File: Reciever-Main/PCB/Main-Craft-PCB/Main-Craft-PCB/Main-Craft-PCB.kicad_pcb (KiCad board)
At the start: 2 copper layers, 96 parts, among them SW4 SW_SPDT, SW5 SW_SPDT, SW6 SW_SPDT, SW7 SW_SPDT, SW8 SW_SPDT, U1 NUCLEO144-F429ZI, U2 LM741, U3 LM741, U4 LM2940-3.0, U5 LM2940-5.0, U6 LM2940-12.0

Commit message: Update PCB and start pon layout
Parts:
- removed R20, R23, R29: 1K, Resistor_SMD:R_0603_1608Metric
- removed R22, R24, R26: 10K, Resistor_SMD:R_0603_1608Metric
- added BT1: Battery, Connector_PinHeader_2.54mm:PinHeader_1x02_P2.54mm_Vertical, F.Cu at (124.5, 55.9)
- added D14: 1N5817, My_library:1N5817M, F.Cu at (55.9, 27.9)
- added J1: nRF24L01_Conn, Connector_PinHeader_2.54mm:PinHeader_2x04_P2.54mm_Vertical_SMD, F.Cu at (170.1, 57.6)
- added J10: L298N, Connector_PinHeader_2.54mm:PinHeader_1x06_P2.54mm_Vertical_SMD_Pin1Left, F.Cu at (124.5, 139.7)
- added J2: IR_SENSOR_1, Connector_PinHeader_2.54mm:PinHeader_1x03_P2.54mm_Vertical_SMD_Pin1Left, F.Cu at (139.7, 144.8)
- added J3: IR_SENSOR_2, Connector_PinHeader_2.54mm:PinHeader_1x03_P2.54mm_Vertical_SMD_Pin1Left, F.Cu at (147.3, 144.8)
- added J4: IR_SENSOR_?, Connector_PinHeader_2.54mm:PinHeader_1x03_P2.54mm_Vertical_SMD_Pin1Left, F.Cu at (132.1, 144.8)
- added J5: IR_SENSOR_?, Connector_PinHeader_2.54mm:PinHeader_1x03_P2.54mm_Vertical_SMD_Pin1Left, F.Cu at (154.9, 144.7)
- added J6: ESC_1, Connector_PinHeader_2.54mm:PinHeader_1x03_P2.54mm_Vertical_SMD_Pin1Left, F.Cu at (185.4, 144.8)
- added J7: ESC_2, Connector_PinHeader_2.54mm:PinHeader_1x03_P2.54mm_Vertical_SMD_Pin1Left, F.Cu at (177.8, 144.8)
- added J8: ESC_3, Connector_PinHeader_2.54mm:PinHeader_1x03_P2.54mm_Vertical_SMD_Pin1Left, F.Cu at (170.2, 144.8)
- added J9: ESC_4, Connector_PinHeader_2.54mm:PinHeader_1x03_P2.54mm_Vertical_SMD_Pin1Left, F.Cu at (162.6, 144.8)
- added Q1: 2N2219, Package_TO_SOT_SMD:SOT-23, F.Cu at (16.1, 15.2)
- added Q10: 2N2219, Package_TO_SOT_SMD:SOT-23, F.Cu at (33.0, 66.0)
- added Q11: 2N2219, Package_TO_SOT_SMD:SOT-23, F.Cu at (84.8, 37.1)
- added Q12: 2N2219, Package_TO_SOT_SMD:SOT-23, F.Cu at (97.5, 39.7)
- added Q13: 2N2219, Package_TO_SOT_SMD:SOT-23, F.Cu at (-82.1, 63.5)
- added Q14: 2N2219, Package_TO_SOT_SMD:SOT-23, F.Cu at (-55.9, 30.5)
- added Q2: 2N2219, Package_TO_SOT_SMD:SOT-23, F.Cu at (33.0, 15.2)
- added Q3: 2N2219, Package_TO_SOT_SMD:SOT-23, F.Cu at (16.0, 27.9)
- added Q4: 2N2219, Package_TO_SOT_SMD:SOT-23, F.Cu at (33.0, 22.9)
- added Q5: 2N2219, Package_TO_SOT_SMD:SOT-23, F.Cu at (20.3, 35.6)
- added Q6: 2N2219, Package_TO_SOT_SMD:SOT-23, F.Cu at (35.6, 33.0)
- added Q7: 2N2219, Package_TO_SOT_SMD:SOT-23, F.Cu at (17.8, 45.7)
- added Q8: 2N2219, Package_TO_SOT_SMD:SOT-23, F.Cu at (20.3, 58.4)
- added Q9: 2N2219, Package_TO_SOT_SMD:SOT-23, F.Cu at (35.6, 48.3)
- added SW1: SW_Push, Button_Switch_SMD:SW_Push_1P1T_NO_6x6mm_H9.5mm, F.Cu at (167.6, 68.6)
- added SW2: SW_Push, Button_Switch_SMD:SW_Push_1P1T_NO_6x6mm_H9.5mm, F.Cu at (167.6, 76.2)
- D17: footprint My_library:1N5817M -> Diode_SMD:D_0603_1608Metric
- SW4, SW5, SW6, SW7, SW8: footprint My_library:KNX-1-D1 -> My_library:JS202011SCQN
- U1: footprint Module:ST_Morpho_Connector_144_STLink -> My_library:MODULE_NUCLEO-F429ZI
- U6: footprint My_library:KNX-1-D1 -> Package_TO_SOT_SMD:SOT-223
- moved R39 229.8 mm to (-72.7, 63.5)
- moved R43 222.7 mm to (-77.8, 66.0)
- moved R49 209.1 mm to (-71.9, 55.9)
- moved C1 207.1 mm to (-55.9, 63.5)
- moved R50 200.8 mm to (-48.3, 43.2)
- moved U2 198.2 mm to (-64.3, 58.4)
- moved C3 196.5 mm to (-64.3, 63.5)
- moved D12 193.1 mm to (-77.0, 58.4)
- moved R44 184.3 mm to (-59.2, 53.3)
- moved R45 183.2 mm to (-48.3, 30.5)
- moved D13 178.5 mm to (-61.0, 38.1)
- moved C2 176.0 mm to (-54.1, 43.2)
- moved RV2 175.3 mm to (-52.2, 36.5)
- moved RV1 170.7 mm to (-54.1, 58.4)
- moved R46 170.2 mm to (-44.0, 27.9)
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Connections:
- R27 pad 2: SW_4 -> SW_5
- R31 pad 2: SW_7 -> SW_4
- R34 pad 2: SW_5 -> SW_6
- R38 pad 2: SW_6 -> SW_5
- U1 pad 125: SW_7 -> unconnected-(U1-Pad125)
- U1 pad 46: MOTOR_2_A -> unconnected-(U1-Pad46)
- U1 pad 47: unconnected-(U1-Pad47) -> MOTOR_2_A
- U1 pad 90: SW_9 -> unconnected-(U1-Pad90)
- U1 pad 97: SW_8 -> unconnected-(U1-Pad97)
- U1 pad 99: MOSI -> MISO
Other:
- board outline added: 68.6 x 99.1 mm

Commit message: Start Routing for tracks on PCB
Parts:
- removed the SW5 at (167.6, 96.5)
- added R20: 1K, Resistor_SMD:R_0603_1608Metric, F.Cu at (172.7, 97.8)
- added R22: 10K, Resistor_SMD:R_0603_1608Metric, F.Cu at (172.7, 94.6)
- added R23: 10K, Resistor_SMD:R_0603_1608Metric, F.Cu at (162.6, 94.6)
- added R24: 1K, Resistor_SMD:R_0603_1608Metric, F.Cu at (162.6, 97.8)
- added SW6: SW_SPDT, My_library:JS202011SCQN, F.Cu at (167.6, 95.9)
- J10: footprint Connector_PinHeader_2.54mm:PinHeader_1x06_P2.54mm_Vertical_SMD_Pin1Left -> Connector_PinHeader_2.54mm:PinHeader_1x06_P2.54mm_Vertical
- J2, J3, J4, J5, J6, J7, J8, J9: footprint Connector_PinHeader_2.54mm:PinHeader_1x03_P2.54mm_Vertical_SMD_Pin1Left -> Connector_PinHeader_2.54mm:PinHeader_1x03_P2.54mm_Vertical
- SW8: footprint My_library:JS202011SCQN -> My_library:KNX-1-D1
- U1: footprint My_library:MODULE_NUCLEO-F429ZI -> My_library:MODULE_NUCLEO-F429ZI_JUST_PINS
- moved Q13 235.9 mm to (153.0, 82.5), turned to 180 degrees
- moved D12 235.7 mm to (158.1, 74.9), turned to 90 degrees
- moved R49 231.1 mm to (158.1, 78.7), turned to -90 degrees
- moved R43 224.6 mm to (146.1, 84.5), turned to 90 degrees
- moved R39 222.3 mm to (149.2, 76.8), turned to 90 degrees
- moved U2 218.8 mm to (153.7, 78.1)
- moved C3 214.2 mm to (149.2, 80.6), turned to 90 degrees
- moved R44 210.7 mm to (149.2, 84.5), turned to 90 degrees
- moved D13 209.5 mm to (145.4, 74.3), turned to 90 degrees
- moved RV1 207.7 mm to (153.0, 72.9), turned to -90 degrees
- moved C1 205.3 mm to (149.2, 72.9), turned to 90 degrees
- moved Q14 202.8 mm to (140.3, 81.9), turned to 180 degrees
- moved R50 196.8 mm to (145.4, 78.1), turned to -90 degrees
- moved RV2 196.2 mm to (140.7, 72.3), turned to -90 degrees
- moved C2 193.5 mm to (137.2, 72.4), turned to -90 degrees
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- renumbered SW6 to SW3, SW7 to SW5
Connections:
- R31 pad 2: SW_4 -> SW_3
- R38 pad 2: SW_5 -> SW_4
- SW4 pad 1: Net-(R26-Pad1) -> unconnected-(SW4-Pad1)
- SW4 pad 3: Net-(R23-Pad1) -> Net-(R27-Pad1)
- U1 pad 109: unconnected-(U1-Pad109) -> BAT_15_PERCENT
- U1 pad 115: BAT_15_PERCENT -> unconnected-(U1-Pad115)
- U1 pad 117: BAT_30_PERCENT -> unconnected-(U1-Pad117)
- U1 pad 122: unconnected-(U1-Pad122) -> SW_7
- U1 pad 127: unconnected-(U1-Pad127) -> SW_8
- U1 pad 38: unconnected-(U1-Pad38) -> BAT_30_PERCENT
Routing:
- net +5V: track 0.00 -> 476.2 mm, vias 0 -> 9
- net +BATT: track 0.00 -> 119.6 mm, vias 0 -> 4
- net BUZZER: track 0.00 -> 80.4 mm
- net MOTOR_1_EN: track 0.00 -> 62.0 mm
- net +3V3: track 0.00 -> 57.7 mm, vias 0 -> 2
- net SW_1: track 0.00 -> 51.6 mm, vias 0 -> 1
- net +12V: track 0.00 -> 50.9 mm
- net SW_4: track 0.00 -> 50.6 mm, vias 0 -> 1
- net SW_2: track 0.00 -> 48.1 mm
- net IR_4: track 0.00 -> 47.8 mm
- net IR_3: track 0.00 -> 46.3 mm
- net Net-(Q6-Pad3): track 0.00 -> 45.8 mm
- net IR_2: track 0.00 -> 44.6 mm
- net IR_1: track 0.00 -> 43.9 mm
- net Net-(Q5-Pad3): track 0.00 -> 39.6 mm
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- added copper zone on B.Cu, net Earth
- added copper zone on F.Cu, net Earth

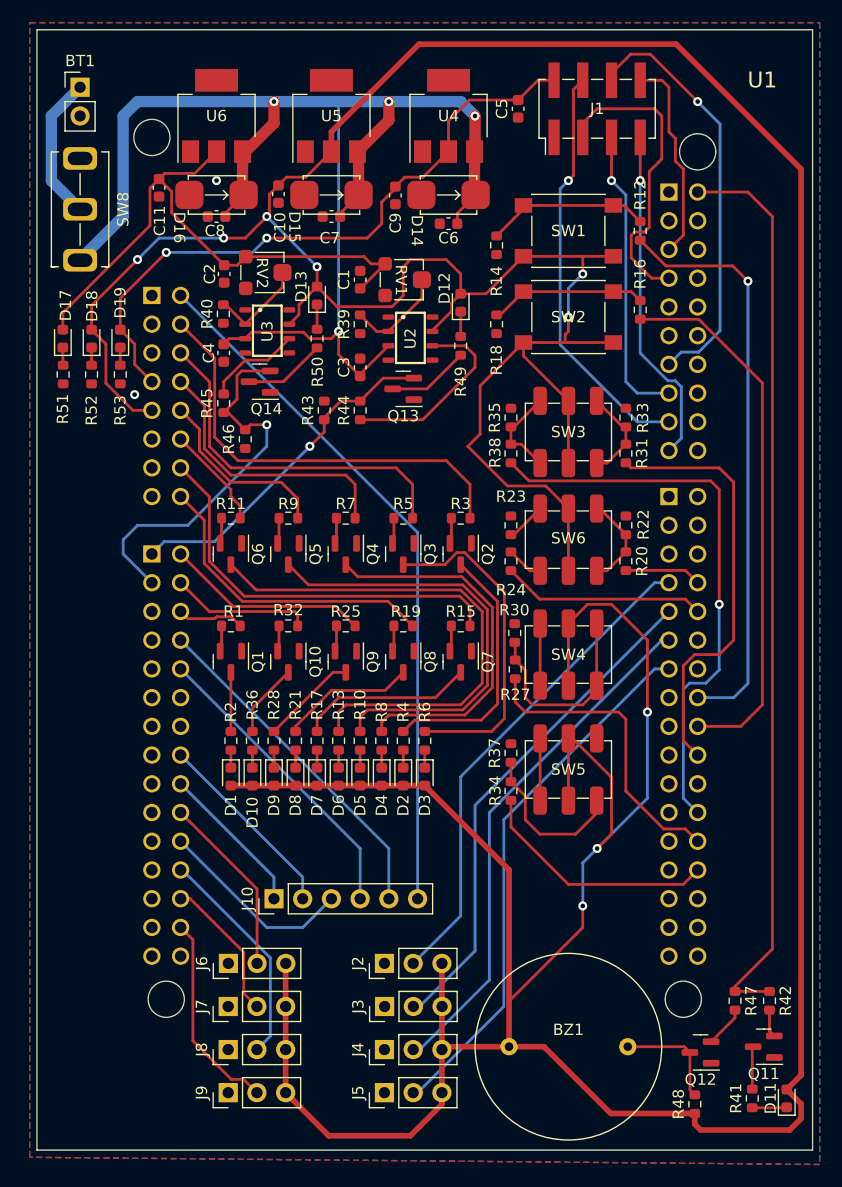
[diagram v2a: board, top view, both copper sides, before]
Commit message: Clear DRC for the PCB
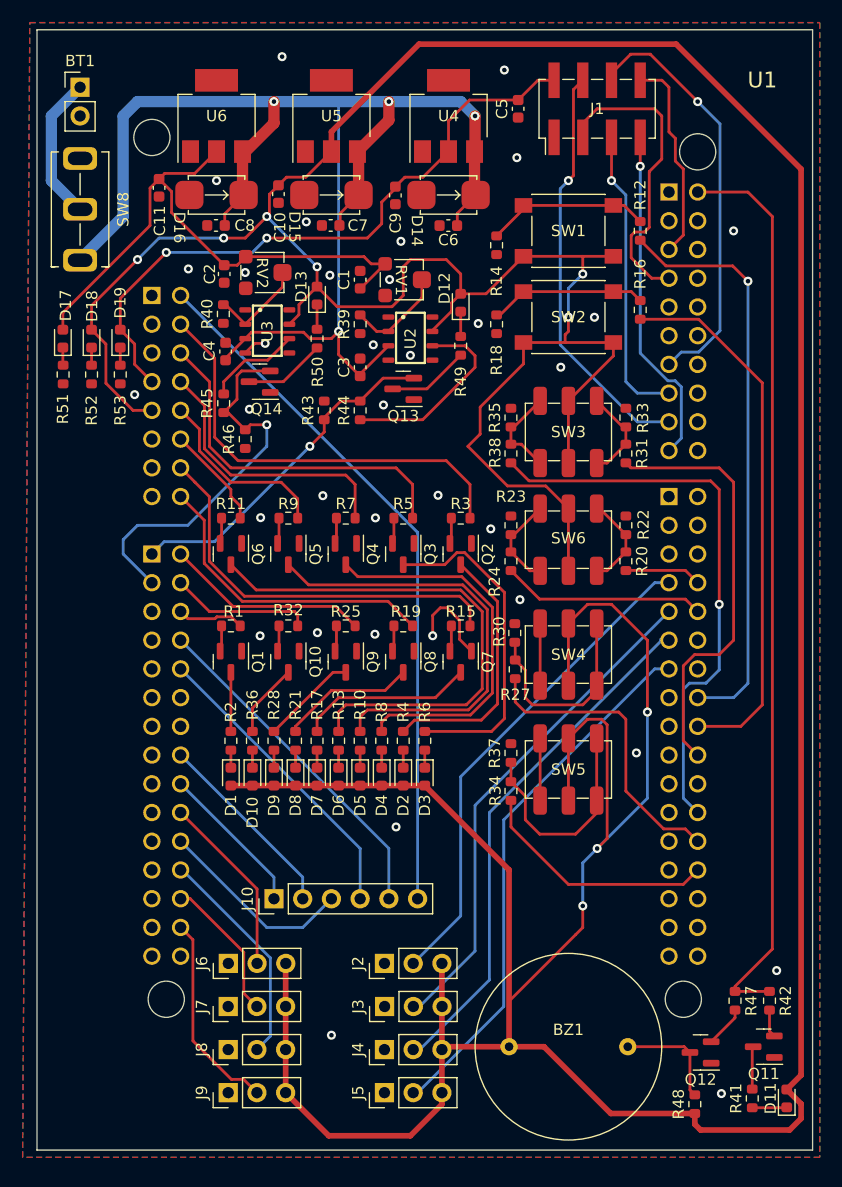
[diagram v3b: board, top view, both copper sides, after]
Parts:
- moved C7 0.79 mm to (146.6, 68.1)
- moved C8 0.79 mm to (136.5, 68.1)
- moved C4 0.21 mm to (137.3, 79.2), turned to 90 degrees
- moved C6 0.17 mm to (157.0, 68.1)
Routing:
- net Earth: track 0.00 -> 10.2 mm, vias 2 -> 35
- net Net-(R34-Pad1): track 14.3 -> 19.8 mm
- net +5V: track 476.2 -> 479.7 mm
- net +BATT: track 119.6 -> 121.7 mm
- net Net-(R23-Pad1): track 6.81 -> 8.06 mm
- net Net-(BT1-Pad1): track 13.5 -> 12.9 mm

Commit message: Finalise PCB
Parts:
- renumbered SW8 to PWR, BT1 to PWR
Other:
- board text added: "+"
- board text added: "-"
- board text added: "0"
- board text added: "1"
- board text added: "12V"
- board text added: "1A"
- board text added: "1B"
- board text added: "1_EN"
- board text added: "2"
- board text added: "2A"
- board text added: "2B"
- board text added: "2_EN"
- board text added: "3"
- board text added: "3V3"
- board text added: "4"
- board text added: "5V"
- board text added: "NUCLEO-F429ZI"
- board text added: "O.R.C.A - Main Board"
- board text added: "nRF24L01"
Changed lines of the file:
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@@
     (property "Sheetname" "")
     (attr through_hole)
-    (fp_text reference "SW8" (at 0 3.81 90 unlocked) (layer "F.SilkS")
+    (fp_text reference "PWR" (at 0 5.08 90 unlocked) (layer "F.SilkS")
       (effects (font (size 1 1) (thickness 0.15)))
     )
@@
     (property "Sheetname" "")
     (attr smd)
-    (fp_text reference "D17" (at 2.933761 0.251495 90) (layer "F.SilkS")
+    (fp_text reference "D17" (at 3.025708 0.007025 90) (layer "F.SilkS")
       (effects (font (size 1 1) (thickness 0.15)))
     )
@@
     (property "Sheetname" "")
     (attr through_hole)
-    (fp_text reference "J4" (at 0 -2.33 90) (layer "F.SilkS")
+    (fp_text reference "J4" (at 0 7.597562 90) (layer "F.SilkS")
       (effects (font (size 1 1) (thickness 0.15)))
     )
@@
     (property "Sheetname" "")
     (attr through_hole)
-    (fp_text reference "J8" (at 0 -2.33 90) (layer "F.SilkS")
+    (fp_text reference "J8" (at -0.031528 -2.442763 90) (layer "F.SilkS")
       (effects (font (size 1 1) (thickness 0.15)))
     )
@@
     (property "Sheetname" "")
     (attr through_hole)
-    (fp_text reference "J2" (at 0 -2.33 90) (layer "F.SilkS")
+    (fp_text reference "J2" (at 0 8.01101 90) (layer "F.SilkS")
       (effects (font (size 1 1) (thickness 0.15)))
     )
@@
     (property "Sheetname" "")
     (attr through_hole)
-    (fp_text reference "J9" (at 0 -2.33 90) (layer "F.SilkS")
+    (fp_text reference "J9" (at 0.006773 -2.48048 90) (layer "F.SilkS")
       (effects (font (size 1 1) (thickness 0.15)))
     )
@@
     (property "Sheetname" "")
     (attr through_hole)
-    (fp_text reference "U1" (at 29.845 -43.815) (layer "F.SilkS")
+    (fp_text reference "U1" (at 29.21 -36.195) (layer "F.SilkS")
       (effects (font (size 1.4 1.4) (thickness 0.15)))
     )
@@
     (property "Sheetname" "")
     (attr through_hole)
-    (fp_text reference "BT1" (at 0 -2.33) (layer "F.SilkS")
+    (fp_text reference "PWR" (at 0 -2.54) (layer "F.SilkS")
       (effects (font (size 1 1) (thickness 0.15)))
     )
@@
     (property "Sheetname" "")
     (attr smd)
-    (fp_text reference "C6" (at 0 1.27) (layer "F.SilkS")
+    (fp_text reference "C6" (at -0.016334 1.51793) (layer "F.SilkS")
       (effects (font (size 1 1) (thickness 0.15)))
     )
@@
     (property "Sheetname" "")
     (attr through_hole)
-    (fp_text reference "J5" (at 0 -2.33 90) (layer "F.SilkS")
+    (fp_text reference "J5" (at 0 7.696792 90) (layer "F.SilkS")
       (effects (font (size 1 1) (thickness 0.15)))
     )
@@
     (property "Sheetname" "")
     (attr smd)
-    (fp_text reference "D18" (at 2.875538 0.043045 90) (layer "F.SilkS")
+    (fp_text reference "D18" (at 3.176312 0.043045 90) (layer "F.SilkS")
       (effects (font (size 1 1) (thickness 0.15)))
     )
@@
     (property "Sheetname" "")
     (attr through_hole)
-    (fp_text reference "J7" (at 0 -2.33 90) (layer "F.SilkS")
+    (fp_text reference "J7" (at 0.043323 -2.405046 90) (layer "F.SilkS")
       (effects (font (size 1 1) (thickness 0.15)))
     )
@@
     (property "Sheetname" "")
     (attr smd)
-    (fp_text reference "D13" (at 0.780778 -1.397764 90) (layer "F.SilkS")
+    (fp_text reference "D13" (at 0.865916 -1.610494 90) (layer "F.SilkS")
       (effects (font (size 1 1) (thickness 0.15)))
     )
@@
     (property "Sheetname" "")
     (attr through_hole)
-    (fp_text reference "J3" (at 0 -2.33 90) (layer "F.SilkS")
+    (fp_text reference "J3" (at 0 7.99601 90) (layer "F.SilkS")
       (effects (font (size 1 1) (thickness 0.15)))
     )
@@
     (property "Sheetname" "")
     (attr through_hole)
-    (fp_text reference "J6" (at 0 -2.33 90) (layer "F.SilkS")
+    (fp_text reference "J6" (at 0.005023 -2.49548 90) (layer "F.SilkS")
       (effects (font (size 1 1) (thickness 0.15)))
     )
@@
     (property "Sheetname" "")
     (attr smd)
-    (fp_text reference "R24" (at 1.806736 1.442446 90) (layer "F.SilkS")
+    (fp_text reference "R24" (at 2.54 0 180) (layer "F.SilkS")
       (effects (font (size 1 1) (thickness 0.15)))
     )
@@
   )
   (gr_rect (start 120.65 50.8) (end 189.23 149.86) (layer "Edge.Cuts") (width 0.1) (fill none))
+  (gr_text "2B" (at 144.165975 130.5106) (layer "F.SilkS")
+    (effects (font (size 1.5 1.5) (thickness 0.3)))
+  )
+  (gr_text "-" (at 127.635 58.42) (layer "F.SilkS")
+    (effects (font (size 1.5 1.5) (thickness 0.3)))
+  )
+  (gr_text "1" (at 148.59 133.35) (layer "F.SilkS")
+    (effects (font (size 1.5 1.5) (thickness 0.3)))
+  )
+  (gr_text "1_EN" (at 155.555428 130.531575) (layer "F.SilkS")
+    (effects (font (size 1.5 1.5) (thickness 0.3)))
+  )
+  (gr_text "O.R.C.A - Main Board" (at 125.095 111.76 90) (layer "F.SilkS")
+    (effects (font (size 1.5 1.5) (thickness 0.3)))
+  )
+  (gr_text "2A" (at 146.685 124.46) (layer "F.SilkS")
+    (effects (font (size 1.5 1.5) (thickness 0.3)))
+  )
+  (gr_text "3" (at 145.415 140.97) (layer "F.SilkS")
+    (effects (font (size 1.5 1.5) (thickness 0.3)))
+  )
+  (gr_text "+\n" (at 127.635 55.88 90) (layer "F.SilkS")
+    (effects (font (size 1.5 1.5) (thickness 0.3)))
+  )
+  (gr_text "5V" (at 146.685 52.705) (layer "F.SilkS")
+    (effects (font (size 1.5 1.5) (thickness 0.3)))
+  )
+  (gr_text "1A" (at 151.765 124.46) (layer "F.SilkS")
+    (effects (font (size 1.5 1.5) (thickness 0.3)))
+  )
+  (gr_text "NUCLEO-F429ZI" (at 182.88 116.84 90) (layer "F.SilkS")
+    (effects (font (size 1.5 1.5) (thickness 0.3)))
+  )
+  (gr_text "2" (at 148.59 137.16) (layer "F.SilkS")
+    (effects (font (size 1.5 1.5) (thickness 0.3)))
+  )
+  (gr_text "3V3" (at 156.845 52.705) (layer "F.SilkS")
+    (effects (font (size 1.5 1.5) (thickness 0.3)))
+  )
+  (gr_text "1B" (at 149.325837 130.489625) (layer "F.SilkS")
+    (effects (font (size 1.5 1.5) (thickness 0.3)))
+  )
+  (gr_text "-\n" (at 128.27 66.675 90) (layer "F.SilkS")
+    (effects (font (size 1.5 1.5) (thickness 0.3)))
+  )
+  (gr_text "1" (at 128.27 70.485) (layer "F.SilkS")
+    (effects (font (size 1.5 1.5) (thickness 0.3)))
+  )
+  (gr_text "2" (at 145.415 137.16) (layer "F.SilkS")
+    (effects (font (size 1.5 1.5) (thickness 0.3)))
+  )
+  (gr_text "12V" (at 136.525 52.705) (layer "F.SilkS")
+    (effects (font (size 1.5 1.5) (thickness 0.3)))
+  )
+  (gr_text "4" (at 145.415 144.78) (layer "F.SilkS")
+    (effects (font (size 1.5 1.5) (thickness 0.3)))
+  )
+  (gr_text "1" (at 145.415 133.35) (layer "F.SilkS")
+    (effects (font (size 1.5 1.5) (thickness 0.3)))
+  )
+  (gr_text "0" (at 128.27 62.23) (layer "F.SilkS")
+    (effects (font (size 1.5 1.5) (thickness 0.3)))
+  )
+  (gr_text "2_EN" (at 140.97 124.46) (layer "F.SilkS")
+    (effects (font (size 1.5 1.5) (thickness 0.3)))
+  )
+  (gr_text "4" (at 148.59 144.78) (layer "F.SilkS")
+    (effects (font (size 1.5 1.5) (thickness 0.3)))
+  )
+  (gr_text "3" (at 148.59 140.97) (layer "F.SilkS")
+    (effects (font (size 1.5 1.5) (thickness 0.3)))
+  )
+  (gr_text "nRF24L01\n" (at 182.245 54.61) (layer "F.SilkS")
+    (effects (font (size 1.5 1.5) (thickness 0.3)))
+  )
   (segment (start 153.67 71.12) (end 156.845 71.12) (width 0.25) (layer "F.Cu") (net 1))
   (segment (start 168.91 130.175) (end 168.91 128.27) (width 0.25) (layer "F.Cu") (net 1))
@@
   (via (at 169.941898 76.218811) (size 0.8) (drill 0.4) (layers "F.Cu" "B.Cu") (free) (net 4))
   (via (at 139.431083 84.350368) (size 0.8) (drill 0.4) (layers "F.Cu" "B.Cu") (free) (net 4))
-  (via (at 146.685 139.7) (size 0.8) (drill 0.4) (layers "F.Cu" "B.Cu") (free) (net 4))
+  (via (at 147.32 146.685) (size 0.8) (drill 0.4) (layers "F.Cu" "B.Cu") (free) (net 4))
   (via (at 161.975979 54.357333) (size 0.8) (drill 0.4) (layers "F.Cu" "B.Cu") (free) (net 4))
   (segment (start 139.62952 77.54048) (end 144.21548 77.54048) (width 0.25) (layer "F.Cu") (net 5))
